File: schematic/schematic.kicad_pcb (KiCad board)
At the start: 2 copper layers, 102 x 86 mm, 23 parts, among them J1 Audio Out, J2 GPIO, J3 Conn_01x02, U1 ESP32-S3-DevKitC, U2 pcm5122module

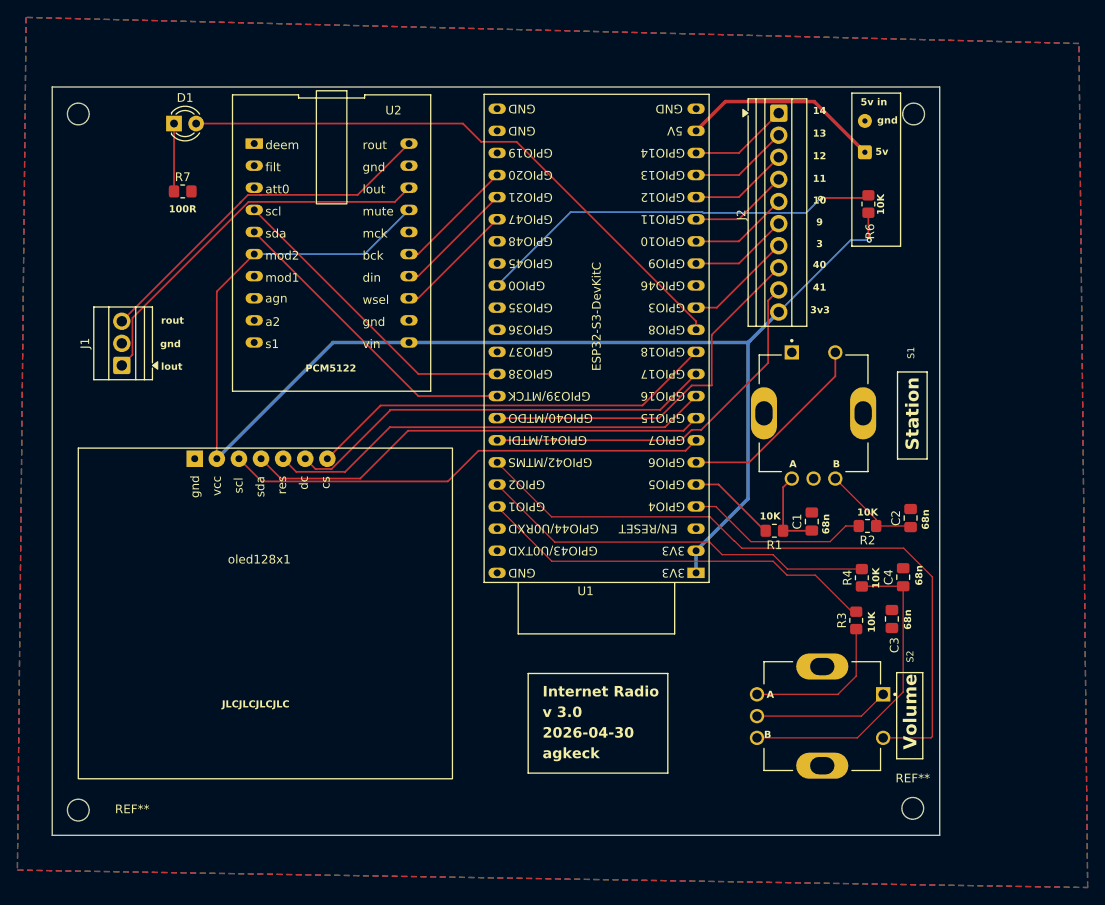
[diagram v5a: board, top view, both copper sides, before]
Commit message: Fixed two islands in the front ground plane by adding vias.
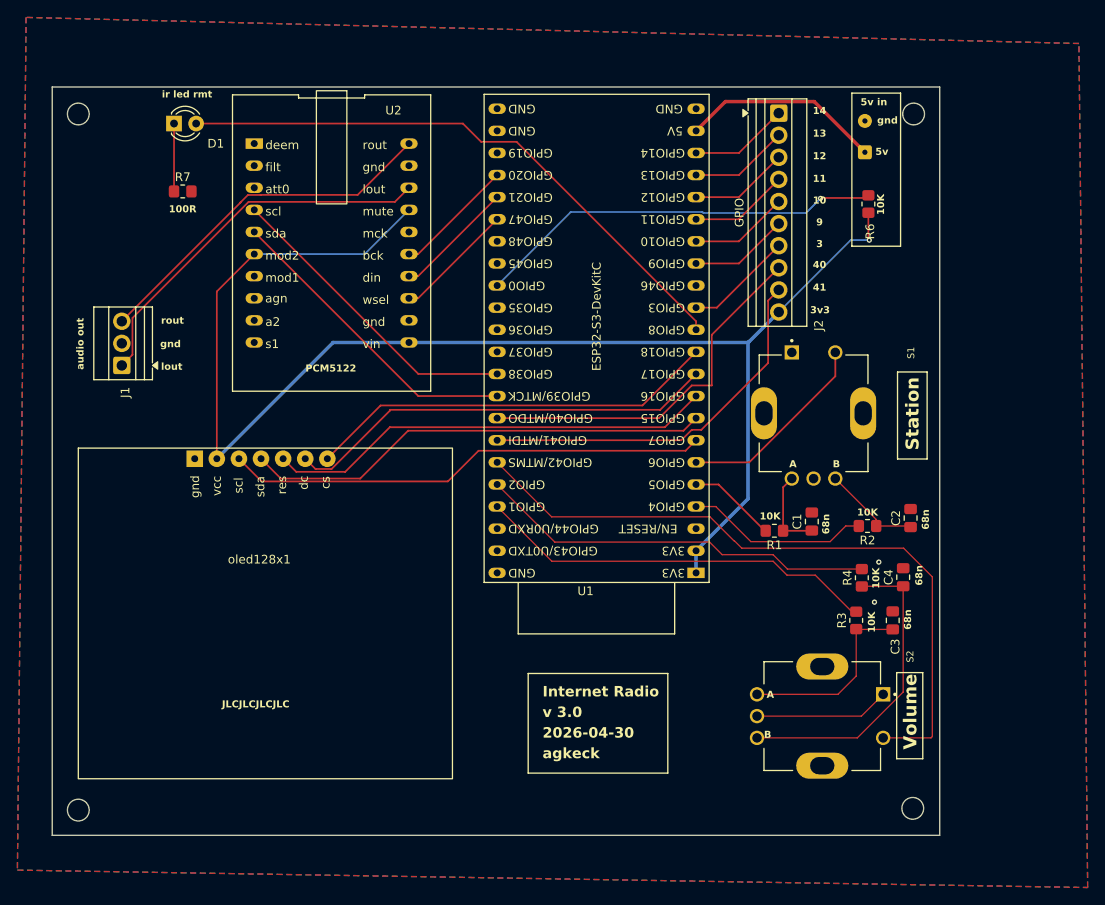
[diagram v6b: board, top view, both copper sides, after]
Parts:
- moved C3 0.19 mm to (134.6, 98.3)
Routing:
- net Net-(C3-Pad1): track 17.7 -> 21.9 mm
- net GND: vias 0 -> 2
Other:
- board text added: "audio out"
- board text added: "ir led rmt"
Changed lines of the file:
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@@
 			(at 6.2 -0.1 0)
 			(layer "F.SilkS")
+			(hide yes)
 			(effects
 				(font
@@
 	(footprint "Capacitor_SMD:C_0805_2012Metric_Pad1.18x1.45mm_HandSolder"
 		(layer "F.Cu")
-		(at 134.5 98.1375 90)
+		(at 134.6 98.3 90)
 		(descr "Capacitor SMD 0805 (2012 Metric), square (rectangular) end terminal, IPC-7351 nominal with elongated pad for handsoldering. (Body size source: IPC-SM-782 page 76, https://www.pcb-3d.com/wordpress/wp-content/uploads/ipc-sm-782a_amendment_1_and_2.pdf, https://docs.google.com/spreadsheets/d/1BsfQQcO9C6DZCsRaXUlFlo91Tg2WpOkGARC1WS5S8t0/edit?usp=sharing), generated with kicad-footprint-generator")
 		(tags "capacitor handsolder")
@@
 		(tags "THT Terminal Block Xinya XY308-2.54-10P pitch 2.54mm size 25.9x6.5mm drill 1.2mm pad 2mm")
 		(property "Reference" "J2"
-			(at 11.7 4.3 90)
+			(at 24.4 -4.6 90)
 			(layer "F.SilkS")
 			(effects
@@
 		(property "Value" "GPIO"
 			(at 11.43 4.52 90)
-			(layer "F.Fab")
+			(layer "F.SilkS")
 			(effects
 				(font
@@
 		(tags "THT Terminal Block Xinya XY308-2.54-3P pitch 2.54mm size 8.12x6.5mm drill 1.2mm pad 2mm")
 		(property "Reference" "J1"
-			(at 2.54 -4.22 90)
+			(at -3.1 0.4 90)
 			(layer "F.SilkS")
 			(effects
@@
 			(at 0 -3.45 0)
 			(layer "F.SilkS")
+			(hide yes)
 			(effects
 				(font
@@
 		(tags "LED IR")
 		(property "Reference" "D1"
-			(at 1.27 -2.96 0)
+			(at 4.8 2.3 0)
 			(layer "F.SilkS")
 			(effects
@@
 		(layer "Edge.Cuts")
 	)
+	(gr_text "ir led rmt"
+		(at 50.6 38.3 0)
+		(layer "F.SilkS")
+		(effects
+			(font
+				(size 0.8 0.8)
+				(thickness 0.16)
+				(bold yes)
+			)
+			(justify left bottom)
+		)
+	)
 	(gr_text "gnd"
 		(at 50.4 67 0)
@@
 		)
 	)
+	(gr_text "audio out"
+		(at 41.7 69.5 90)
+		(layer "F.SilkS")
+		(effects
+			(font
+				(size 0.8128 0.8128)
+				(thickness 0.1524)
+				(bold yes)
+			)
+			(justify left bottom)
+		)
+	)
 	(gr_text "68n"
 		(at 127.4 88.4 90)
@@
 		(net 1)
 	)
+	(via
+		(at 132.5 96.2)
+		(size 0.6)
+		(drill 0.3)
+		(layers "F.Cu" "B.Cu")
+		(free yes)
+		(net 1)
+	)
+	(via
+		(at 133 91.6)
+		(size 0.6)
+		(drill 0.3)
+		(layers "F.Cu" "B.Cu")
+		(free yes)
+		(net 1)
+	)
 	(segment
 		(start 119 106.8)
@@
 	)
 	(segment
+		(start 130.4375 99.3375)
+		(end 130.4 99.3)
+		(width 0.127)
+		(layer "F.Cu")
+		(net 2)
+	)
+	(segment
 		(start 130.4 104.7)
 		(end 130.4 99.3)
@@
 	)
 	(segment
+		(start 134.6 99.3375)
+		(end 130.4375 99.3375)
+		(width 0.127)
+		(layer "F.Cu")
+		(net 2)
+	)
+	(segment
 		(start 128.3 106.8)
 		(end 130.4 104.7)
@@
 		(min_thickness 0.25)
 		(filled_areas_thickness no)
-		(fill
+		(fill yes
 			(thermal_gap 0.5)
 			(thermal_bridge_width 0.5)
